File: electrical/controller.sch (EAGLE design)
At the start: 44 parts, among them IC1 555, IC2 MCP4728, J3 455-1750-1-ND, Q1 DMP3098, Q2 DMG3402L-7, Q3 600mA/40V, Q4 DMP3098, U1 U3V16F15, U2 U3V16F15, U5 MCP6042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

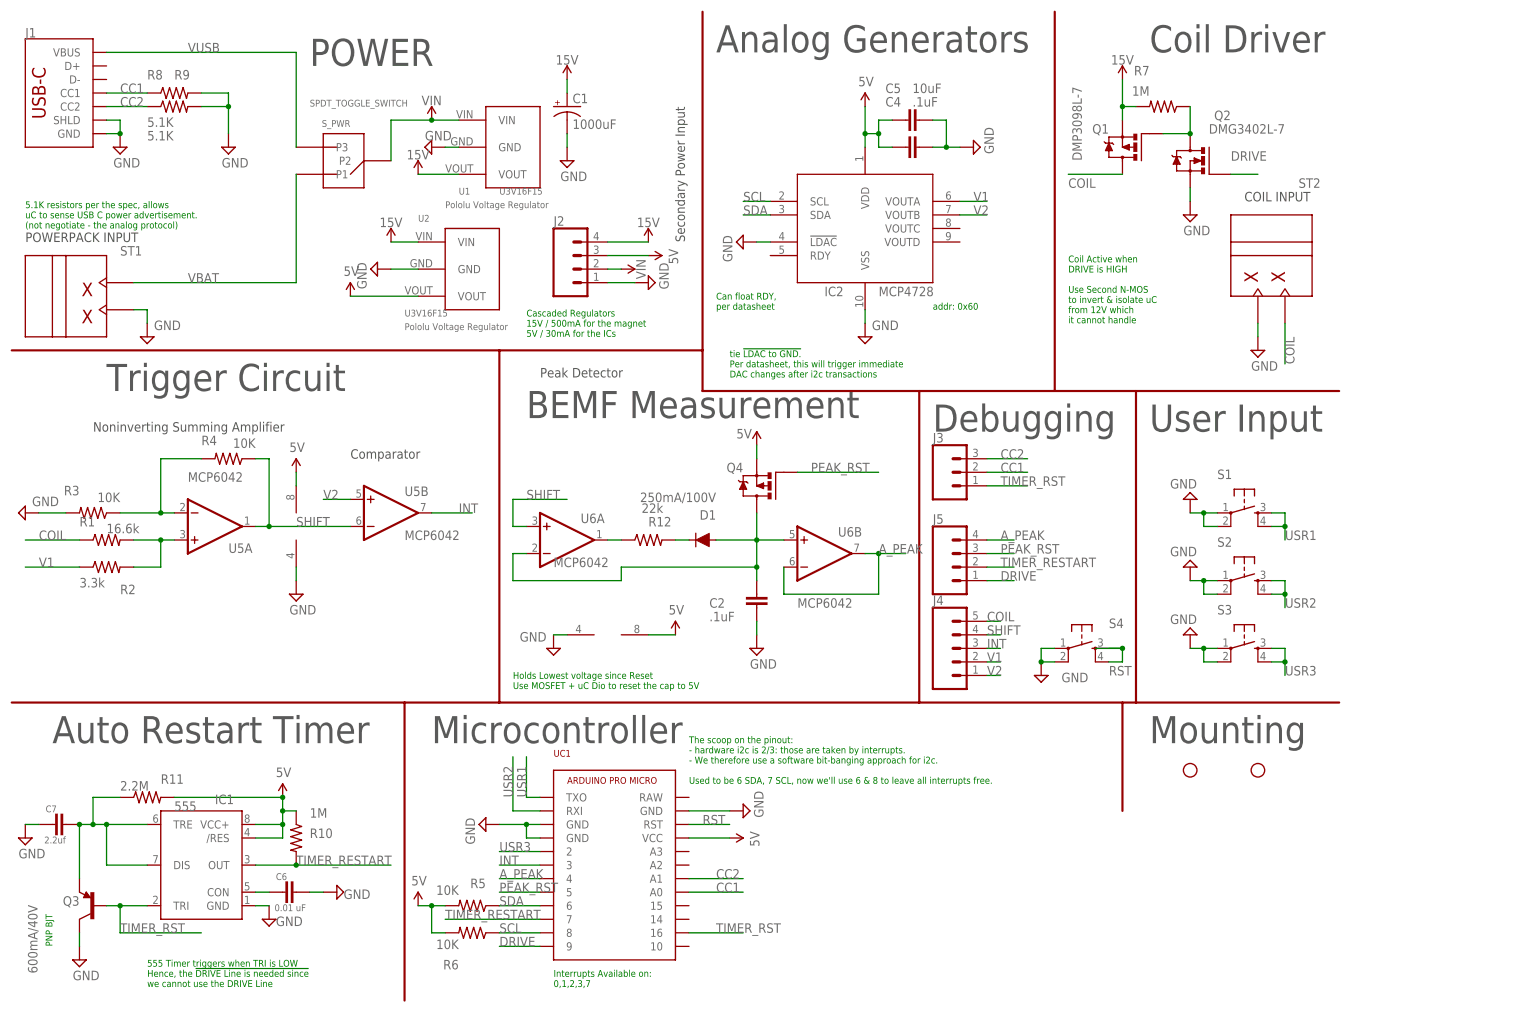
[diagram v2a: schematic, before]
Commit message: Added resistor arrays + other minor erratta, ready for prod
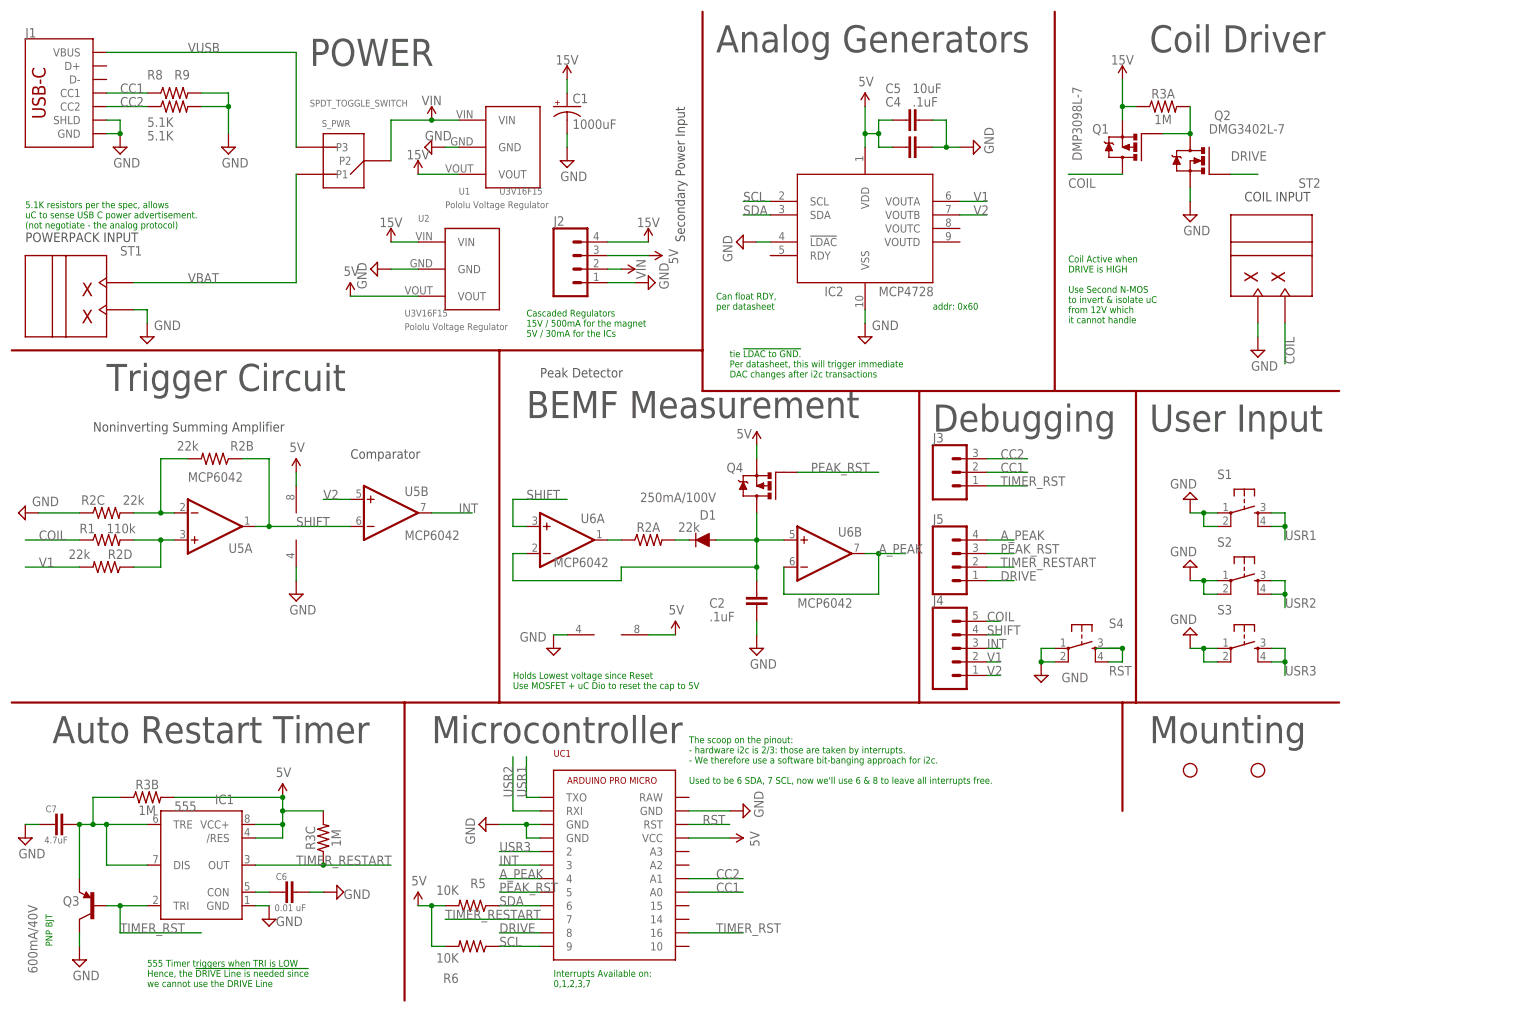
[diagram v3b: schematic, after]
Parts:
- removed R10, R7: 1M, pie:R-US_R0603
- removed R11: 2.2M, pie:R-US_R0603
- removed R12: 22k, pie:R-US_R0603
- removed R4: 10K, pie:R-US_R0603
- C7: value 2.2uf -> 4.7uF
- R1: value 16.6k -> 110k
- R2: value 3.3k -> 22k; device pie:R-US_R0603 -> BEST_Custom:RESISTOR_ARRAY_(4)-2012-1/8W-5%
- R3: value 10K -> 1M; device pie:R-US_R0603 -> BEST_Custom:RESISTOR_ARRAY_(4)-2012-1/8W-5%
- U5, U6: device linear:MCP602SN -> BEST_Custom:MCP602SN
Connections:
- net 15V: now also R3A.1; no longer R7.2
- net 5V: now also R3B.2, R3C.2; no longer R10.1, R11.2
- net DRIVE: now also R3A.2, UC1.8; no longer R7.1, UC1.9
- net GND: now also R2C.1; no longer R3.2
- net N$2: now also R2A.1; no longer R12.1
- net N$3: now also R2A.2; no longer R12.2
- net N$4: now also R2D.1; no longer R2.2
- net N$5: now also R2B.2, R2C.2; no longer R3.1, R4.2
- net N$7: now also R3B.1; no longer R11.1
- net SCL: now also UC1.9; no longer UC1.8
- net SHIFT: now also R2B.1; no longer R4.1
- net TIMER_RESTART: now also R3C.1; no longer R10.2
- net V1: now also R2D.2; no longer R2.1
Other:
- note added: "Stage 1: V+ = R1*V1 + R2*Vcoil / (R1 + R2) Choose R2 = 22k. (For part unification) Solve for Values by solving simultaneous equations: 1) Set Coil = 0, choose V+ = 1V ==> VShift = 2V 2) Set Coil = 3, choose V+ = 1.5V ==> VShift = 3V Previous 5V coil operation chose Coil = 1, V+ = 1.5 (approx 3x the coil count, 1/3 the gain), all resistors 10k. (Actually it's 2.69x the coil count, todo adjust late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"
- note added: "Stage 2: VShift = 1 + (R4/R3) V- Choose R4=R3=22k (for part unification) VShift = 2 V-"
- note added: "Stage 3: Use spare op-amp As comparator to DAC voltage To trigger @ zero crossing."
- note removed: "Stage 1: V+ = R1*V1 + R2*Vcoil / (R1 + R2) Choose R1+R2 = 10k. Solve for Values by solving simultaneous equations: 1) Set Coil = 0, choose V+ = 1V ==> VShift = 2V 2) Set Coil = 3, choose V+ = 1.5V ==> VShift = 3V Previous 5V coil operation chose Coil = 1, V+ = 1.5 (approx 3x the coil count, 1/3 the gain) (Actually it's 2.69x the coil count, todo adjust later)"
- note removed: "Stage 2: VShift = 1 + (R4/R3) V- VShift = 2 V-"
- moved on the sheet: R6

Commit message: Add missing pullup; tweak slots for JLCPCB fab
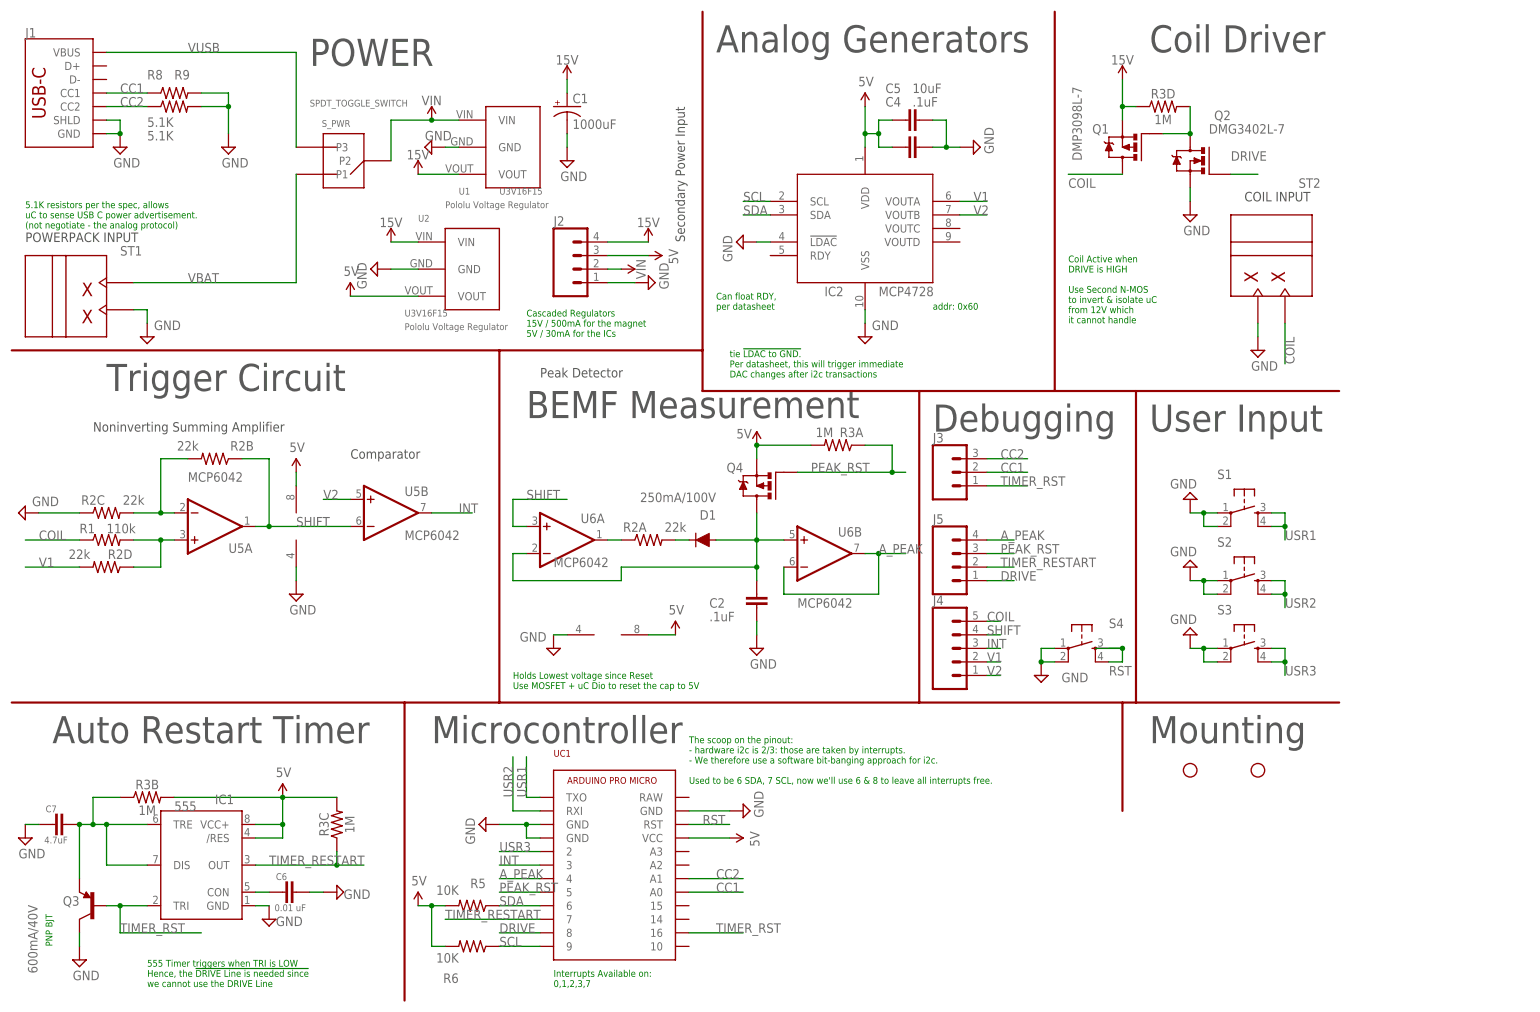
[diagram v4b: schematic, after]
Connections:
- net 15V: now also R3D.1; no longer R3A.1
- net 5V: now also R3A.2
- net DRIVE: now also R3D.2; no longer R3A.2
- net PEAK_RST: now also R3A.1
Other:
- moved on the sheet: R3A, R3C
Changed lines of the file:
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@@
 <attribute name="REVISION" value="D2"/>
 </part>
-<part name="UC1" library="BEST_Custom" library_urn="urn:adsk.eagle:library:10805467" deviceset="ARDUINO_PRO_MICRO" device="2D" package3d_urn="urn:adsk.eagle:package:49177699/1"/>
+<part name="UC1" library="BEST_Custom" library_urn="urn:adsk.eagle:library:10805467" deviceset="ARDUINO_PRO_MICRO" device="2D" package3d_urn="urn:adsk.eagle:package:49177699/2"/>
 <part name="ST1" library="BEST_Custom" library_urn="urn:adsk.eagle:library:10805467" deviceset="2PIN_SCREW" device="" package3d_urn="urn:adsk.eagle:package:49052268/3"/>
 <part name="ST2" library="BEST_Custom" library_urn="urn:adsk.eagle:library:10805467" deviceset="2PIN_SCREW" device="" package3d_urn="urn:adsk.eagle:package:49052268/3"/>
-<part name="U5" library="BEST_Custom" library_urn="urn:adsk.eagle:library:10805467" deviceset="MCP602" device="SN" package3d_urn="urn:adsk.eagle:package:16404/2" value="MCP6042"/>
+<part name="U5" library="BEST_Custom" library_urn="urn:adsk.eagle:library:10805467" deviceset="MCP602" device="SN" package3d_urn="urn:adsk.eagle:package:49204900/1" value="MCP6042"/>
 <part name="SUPPLY1" library="pie" deviceset="GND" device=""/>
 <part name="SUPPLY3" library="pie" deviceset="GND" device=""/>
@@
 <part name="STANDOFF1" library="BEST_Custom" library_urn="urn:adsk.eagle:library:10805467" deviceset="STAND-OFF" device="KEYSTONE_SMT_STANDOFF" package3d_urn="urn:adsk.eagle:package:49038533/2"/>
 <part name="STANDOFF2" library="BEST_Custom" library_urn="urn:adsk.eagle:library:10805467" deviceset="STAND-OFF" device="KEYSTONE_SMT_STANDOFF" package3d_urn="urn:adsk.eagle:package:49038533/2"/>
-<part name="J1" library="BEST_Custom" library_urn="urn:adsk.eagle:library:10805467" deviceset="USB_C" device="_2-LAYER_PADS" package3d_urn="urn:adsk.eagle:package:49053406/2"/>
+<part name="J1" library="BEST_Custom" library_urn="urn:adsk.eagle:library:10805467" deviceset="USB_C" device="_2-LAYER_PADS" package3d_urn="urn:adsk.eagle:package:49053406/4"/>
 <part name="R8" library="pie" deviceset="R-US_" device="R0603" value="5.1K"/>
 <part name="R9" library="pie" deviceset="R-US_" device="R0603" value="5.1K"/>
@@
 <part name="SUPPLY27" library="pie" deviceset="GND" device=""/>
 <part name="SUPPLY25" library="SparkFun-PowerSymbols" deviceset="VIN" device=""/>
-<part name="U6" library="BEST_Custom" library_urn="urn:adsk.eagle:library:10805467" deviceset="MCP602" device="SN" package3d_urn="urn:adsk.eagle:package:16404/2" value="MCP6042"/>
+<part name="U6" library="BEST_Custom" library_urn="urn:adsk.eagle:library:10805467" deviceset="MCP602" device="SN" package3d_urn="urn:adsk.eagle:package:49204900/1" value="MCP6042"/>
 <part name="U$1" library="pie" deviceset="5V" device=""/>
 <part name="SUPPLY28" library="pie" deviceset="GND" device=""/>
@@
 <part name="J5" library="SparkFun-Connectors" library_urn="urn:adsk.eagle:library:49052309" deviceset="CONN_04" device="PTH" package3d_urn="urn:adsk.eagle:package:49052925/1"/>
 <part name="J3" library="SparkFun-Connectors" library_urn="urn:adsk.eagle:library:49052309" deviceset="CONN_03" device="" package3d_urn="urn:adsk.eagle:package:49052910/1" value="455-1750-1-ND"/>
-<part name="R2" library="BEST_Custom" library_urn="urn:adsk.eagle:library:10805467" deviceset="RESISTOR_ARRAY_(4)" device="-2012-1/8W-5%" package3d_urn="urn:adsk.eagle:package:49177700/2" value="22k"/>
-<part name="R3" library="BEST_Custom" library_urn="urn:adsk.eagle:library:10805467" deviceset="RESISTOR_ARRAY_(4)" device="-2012-1/8W-5%" package3d_urn="urn:adsk.eagle:package:49177700/2" value="1M"/>
+<part name="R2" library="BEST_Custom" library_urn="urn:adsk.eagle:library:10805467" deviceset="RESISTOR_ARRAY_(4)" device="-2012-1/8W-5%" package3d_urn="urn:adsk.eagle:package:49177700/3" value="22k"/>
+<part name="R3" library="BEST_Custom" library_urn="urn:adsk.eagle:library:10805467" deviceset="RESISTOR_ARRAY_(4)" device="-2012-1/8W-5%" package3d_urn="urn:adsk.eagle:package:49177700/3" value="1M"/>
 </parts>
 <sheets>
@@
 </instance>
 <instance part="R2" gate="A" x="119.38" y="86.36" smashed="yes">
-<attribute name="NAME" x="119.38" y="87.884" size="1.778" layer="95" font="vector" align="bottom-center"/>
-<attribute name="VALUE" x="127" y="87.884" size="1.778" layer="96" font="vector" rot="R180" align="top-center"/>
+<attribute name="NAME" x="116.84" y="87.884" size="1.778" layer="95" font="vector" align="bottom-center"/>
+<attribute name="VALUE" x="124.46" y="87.884" size="1.778" layer="96" font="vector" rot="R180" align="top-center"/>
 </instance>
 <instance part="R2" gate="B" x="38.1" y="101.6" smashed="yes" rot="R180">
@@
 <attribute name="VALUE" x="12.7" y="82.804" size="1.778" layer="96" font="vector" rot="R180" align="top-center"/>
 </instance>
-<instance part="R3" gate="A" x="215.9" y="167.64" smashed="yes">
-<attribute name="NAME" x="215.9" y="169.164" size="1.778" layer="95" font="vector" align="bottom-center"/>
-<attribute name="VALUE" x="215.9" y="166.116" size="1.778" layer="96" font="vector" align="top-center"/>
+<instance part="R3" gate="A" x="154.94" y="104.14" smashed="yes" rot="R180">
+<attribute name="NAME" x="157.48" y="105.664" size="1.778" layer="95" font="vector" align="bottom-center"/>
+<attribute name="VALUE" x="152.4" y="105.664" size="1.778" layer="96" font="vector" rot="R180" align="top-center"/>
 </instance>
 <instance part="R3" gate="B" x="25.4" y="38.1" smashed="yes">
@@
 <attribute name="VALUE" x="25.4" y="36.576" size="1.778" layer="96" font="vector" align="top-center"/>
 </instance>
-<instance part="R3" gate="C" x="58.42" y="30.48" smashed="yes" rot="R90">
-<attribute name="NAME" x="56.896" y="30.48" size="1.778" layer="95" font="vector" rot="R90" align="bottom-center"/>
-<attribute name="VALUE" x="59.944" y="30.48" size="1.778" layer="96" font="vector" rot="R90" align="top-center"/>
+<instance part="R3" gate="C" x="60.96" y="33.02" smashed="yes" rot="R90">
+<attribute name="NAME" x="59.436" y="33.02" size="1.778" layer="95" font="vector" rot="R90" align="bottom-center"/>
+<attribute name="VALUE" x="62.484" y="33.02" size="1.778" layer="96" font="vector" rot="R90" align="top-center"/>
+</instance>
+<instance part="R3" gate="D" x="215.9" y="167.64" smashed="yes">
+<attribute name="NAME" x="215.9" y="169.164" size="1.778" layer="95" font="vector" align="bottom-center"/>
+<attribute name="VALUE" x="215.9" y="166.116" size="1.778" layer="96" font="vector" align="top-center"/>
 </instance>
 </instances>
@@
 <wire x1="45.72" y1="33.02" x2="50.8" y2="33.02" width="0.1524" layer="91"/>
 <pinref part="U$8" gate="G$1" pin="5V"/>
-<wire x1="50.8" y1="33.02" x2="50.8" y2="35.56" width="0.1524" layer="91"/>
 <pinref part="IC1" gate="G$1" pin="/RES"/>
-<wire x1="50.8" y1="35.56" x2="50.8" y2="38.1" width="0.1524" layer="91"/>
+<wire x1="50.8" y1="33.02" x2="50.8" y2="38.1" width="0.1524" layer="91"/>
 <wire x1="45.72" y1="30.48" x2="50.8" y2="30.48" width="0.1524" layer="91"/>
 <wire x1="50.8" y1="30.48" x2="50.8" y2="33.02" width="0.1524" layer="91"/>
 <junction x="50.8" y="33.02"/>
-<wire x1="58.42" y1="35.56" x2="50.8" y2="35.56" width="0.1524" layer="91"/>
-<junction x="50.8" y="35.56"/>
 <wire x1="30.48" y1="38.1" x2="50.8" y2="38.1" width="0.1524" layer="91"/>
 <junction x="50.8" y="38.1"/>
 <pinref part="R3" gate="B" pin="2"/>
 <pinref part="R3" gate="C" pin="2"/>
+<wire x1="50.8" y1="38.1" x2="60.96" y2="38.1" width="0.1524" layer="91"/>
 </segment>
 <segment>
@@
 <pinref part="U$2" gate="G$1" pin="5V"/>
 <wire x1="139.7" y1="104.14" x2="139.7" y2="101.6" width="0.1524" layer="91"/>
+<wire x1="149.86" y1="104.14" x2="139.7" y2="104.14" width="0.1524" layer="91"/>
+<junction x="139.7" y="104.14"/>
+<pinref part="R3" gate="A" pin="2"/>
 </segment>
 <segment>
@@
 <pinref part="Q1" gate="G$1" pin="G"/>
 <pinref part="Q2" gate="G$1" pin="D"/>
-<pinref part="R3" gate="A" pin="2"/>
+<pinref part="R3" gate="D" pin="2"/>
 </segment>
 <segment>
@@
 <segment>
 <pinref part="Q4" gate="G$1" pin="G"/>
-<wire x1="147.32" y1="99.06" x2="162.56" y2="99.06" width="0.1524" layer="91"/>
+<wire x1="147.32" y1="99.06" x2="165.1" y2="99.06" width="0.1524" layer="91"/>
 <label x="149.86" y="99.06" size="1.778" layer="95"/>
+<wire x1="165.1" y1="99.06" x2="167.64" y2="99.06" width="0.1524" layer="91"/>
+<junction x="165.1" y="99.06"/>
+<pinref part="R3" gate="A" pin="1"/>
+<wire x1="160.02" y1="104.14" x2="165.1" y2="104.14" width="0.1524" layer="91"/>
+<wire x1="165.1" y1="104.14" x2="165.1" y2="99.06" width="0.1524" layer="91"/>
 </segment>
 <segment>
@@
 <junction x="208.28" y="167.64"/>
 <pinref part="SUPPLY26" gate="G$1" pin="12V"/>
-<pinref part="R3" gate="A" pin="1"/>
+<pinref part="R3" gate="D" pin="1"/>
 </segment>
 <segment>
@@
 <net name="TIMER_RESTART" class="0">
 <segment>
-<pinref part="IC1" gate="G$1" pin="OUT"/>
-<label x="53.34" y="25.4" size="1.778" layer="95"/>
-<wire x1="45.72" y1="25.4" x2="58.42" y2="25.4" width="0.1524" layer="91"/>
-<pinref part="R3" gate="C" pin="1"/>
-<wire x1="58.42" y1="25.4" x2="71.12" y2="25.4" width="0.1524" layer="91"/>
-<junction x="58.42" y="25.4"/>
-</segment>
-<segment>
 <pinref part="UC1" gate="APM" pin="7"/>
 <wire x1="99.06" y1="15.24" x2="81.28" y2="15.24" width="0.1524" layer="91"/>
@@
 <pinref part="J5" gate="J1" pin="2"/>
 </segment>
-</net>
+<segment>
+<pinref part="IC1" gate="G$1" pin="OUT"/>
+<wire x1="45.72" y1="25.4" x2="60.96" y2="25.4" width="0.1524" layer="91"/>
+<label x="48.26" y="25.4" size="1.778" layer="95"/>
+<pinref part="R3" gate="C" pin="1"/>
+<wire x1="60.96" y1="25.4" x2="66.04" y2="25.4" width="0.1524" layer="91"/>
+<wire x1="60.96" y1="27.94" x2="60.96" y2="25.4" width="0.1524" layer="91"/>
+<junction x="60.96" y="25.4"/>
+</segment>
+</net>

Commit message: Test which pins can do change interrupts and label SCH
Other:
- note added: "Interrupts Available on: 0,1,2,3,7 0 thru 3 fully functional; 7 can do FALLING but not CHANGE"
- note removed: "Interrupts Available on: 0,1,2,3,7"
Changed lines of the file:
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@@
 <wire x1="91.44" y1="55.88" x2="170.18" y2="55.88" width="0.4064" layer="94"/>
 <text x="213.36" y="48.26" size="5.08" layer="97">Mounting</text>
-<text x="101.6" y="2.54" size="1.27" layer="91">Interrupts Available on:
-0,1,2,3,7</text>
+<text x="96.52" y="2.54" size="1.27" layer="91">Interrupts Available on:  0,1,2,3,7
+0 thru 3 fully functional; 7 can do FALLING but not CHANGE</text>
 <text x="127" y="40.64" size="1.27" layer="91">The scoop on the pinout:
 - hardware i2c is 2/3: those are taken by interrupts.
